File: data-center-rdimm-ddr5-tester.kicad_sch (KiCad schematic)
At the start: 2 parts

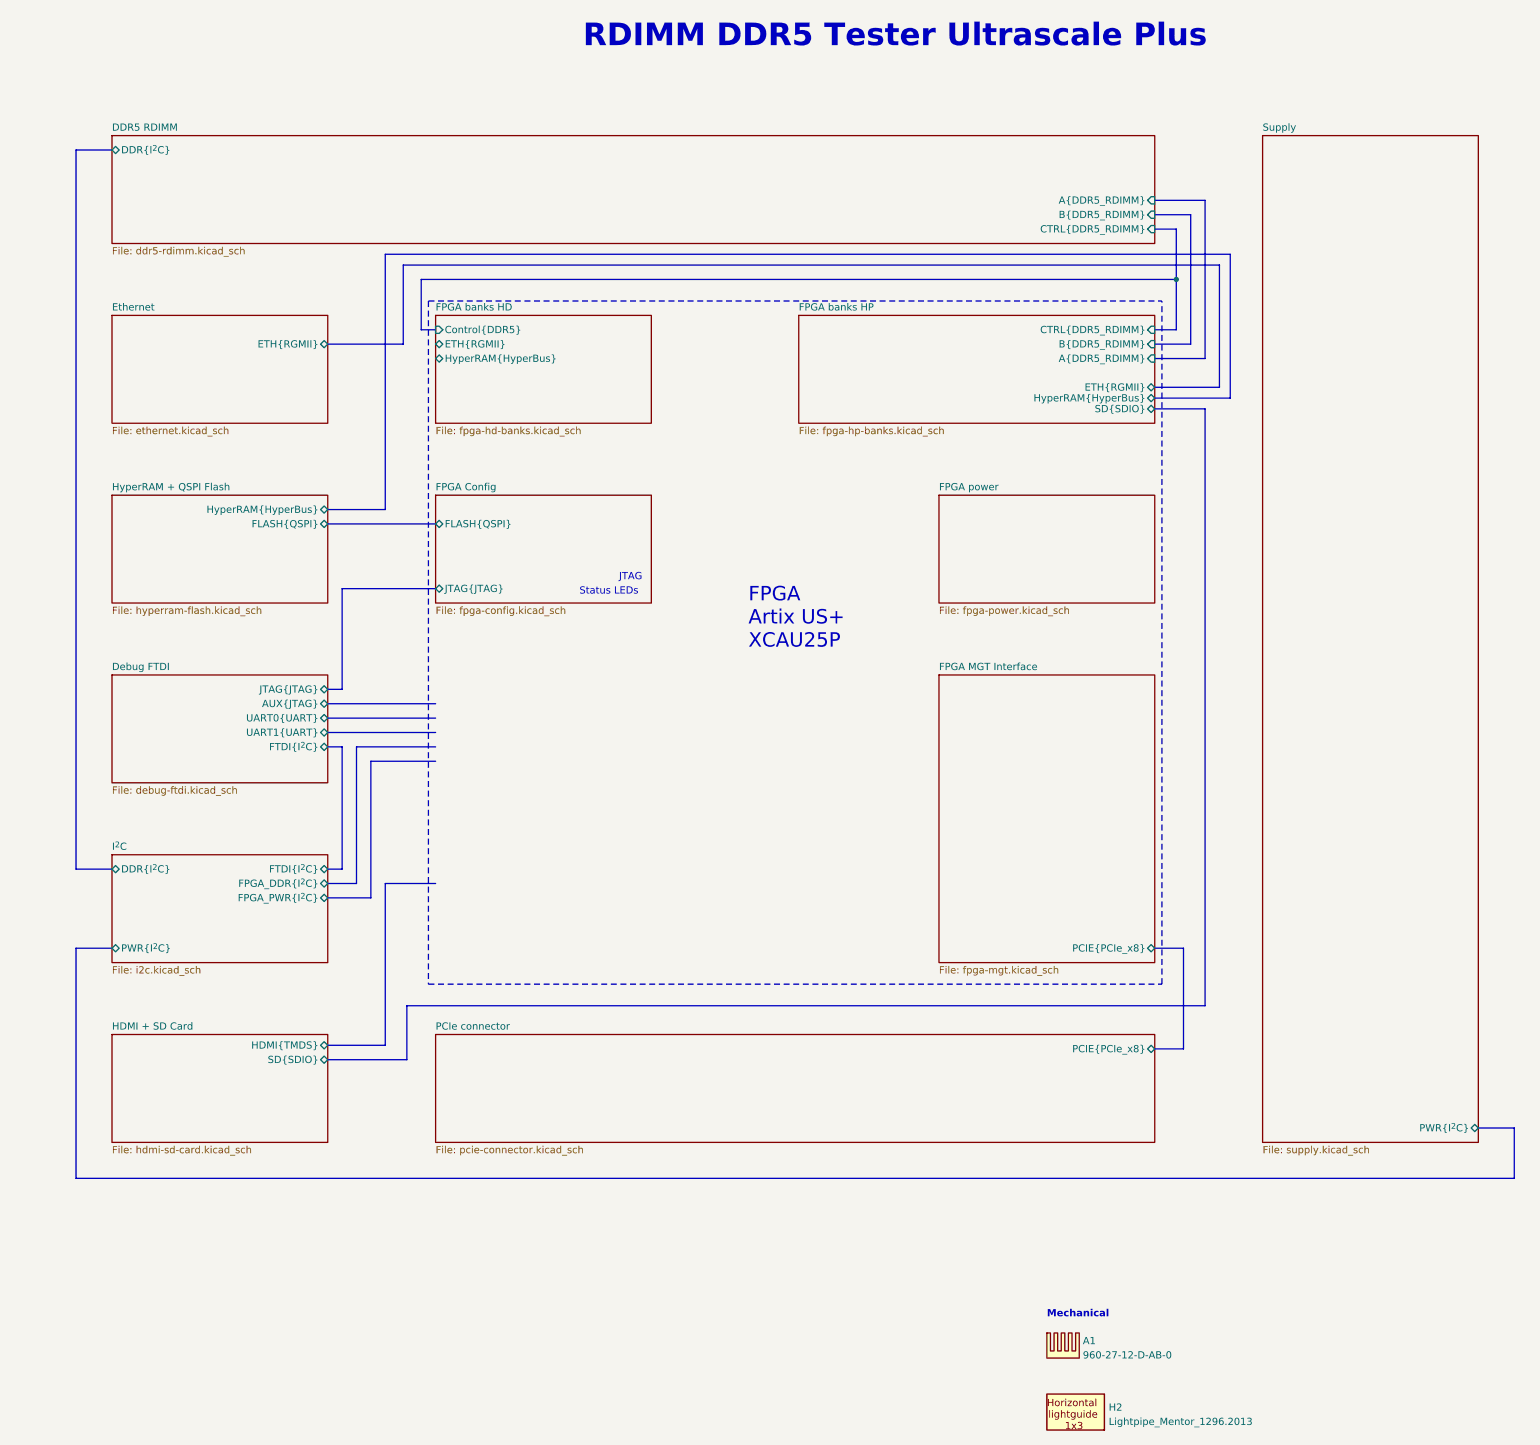
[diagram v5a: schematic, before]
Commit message: [#66312] Continued HDMI schematic connections
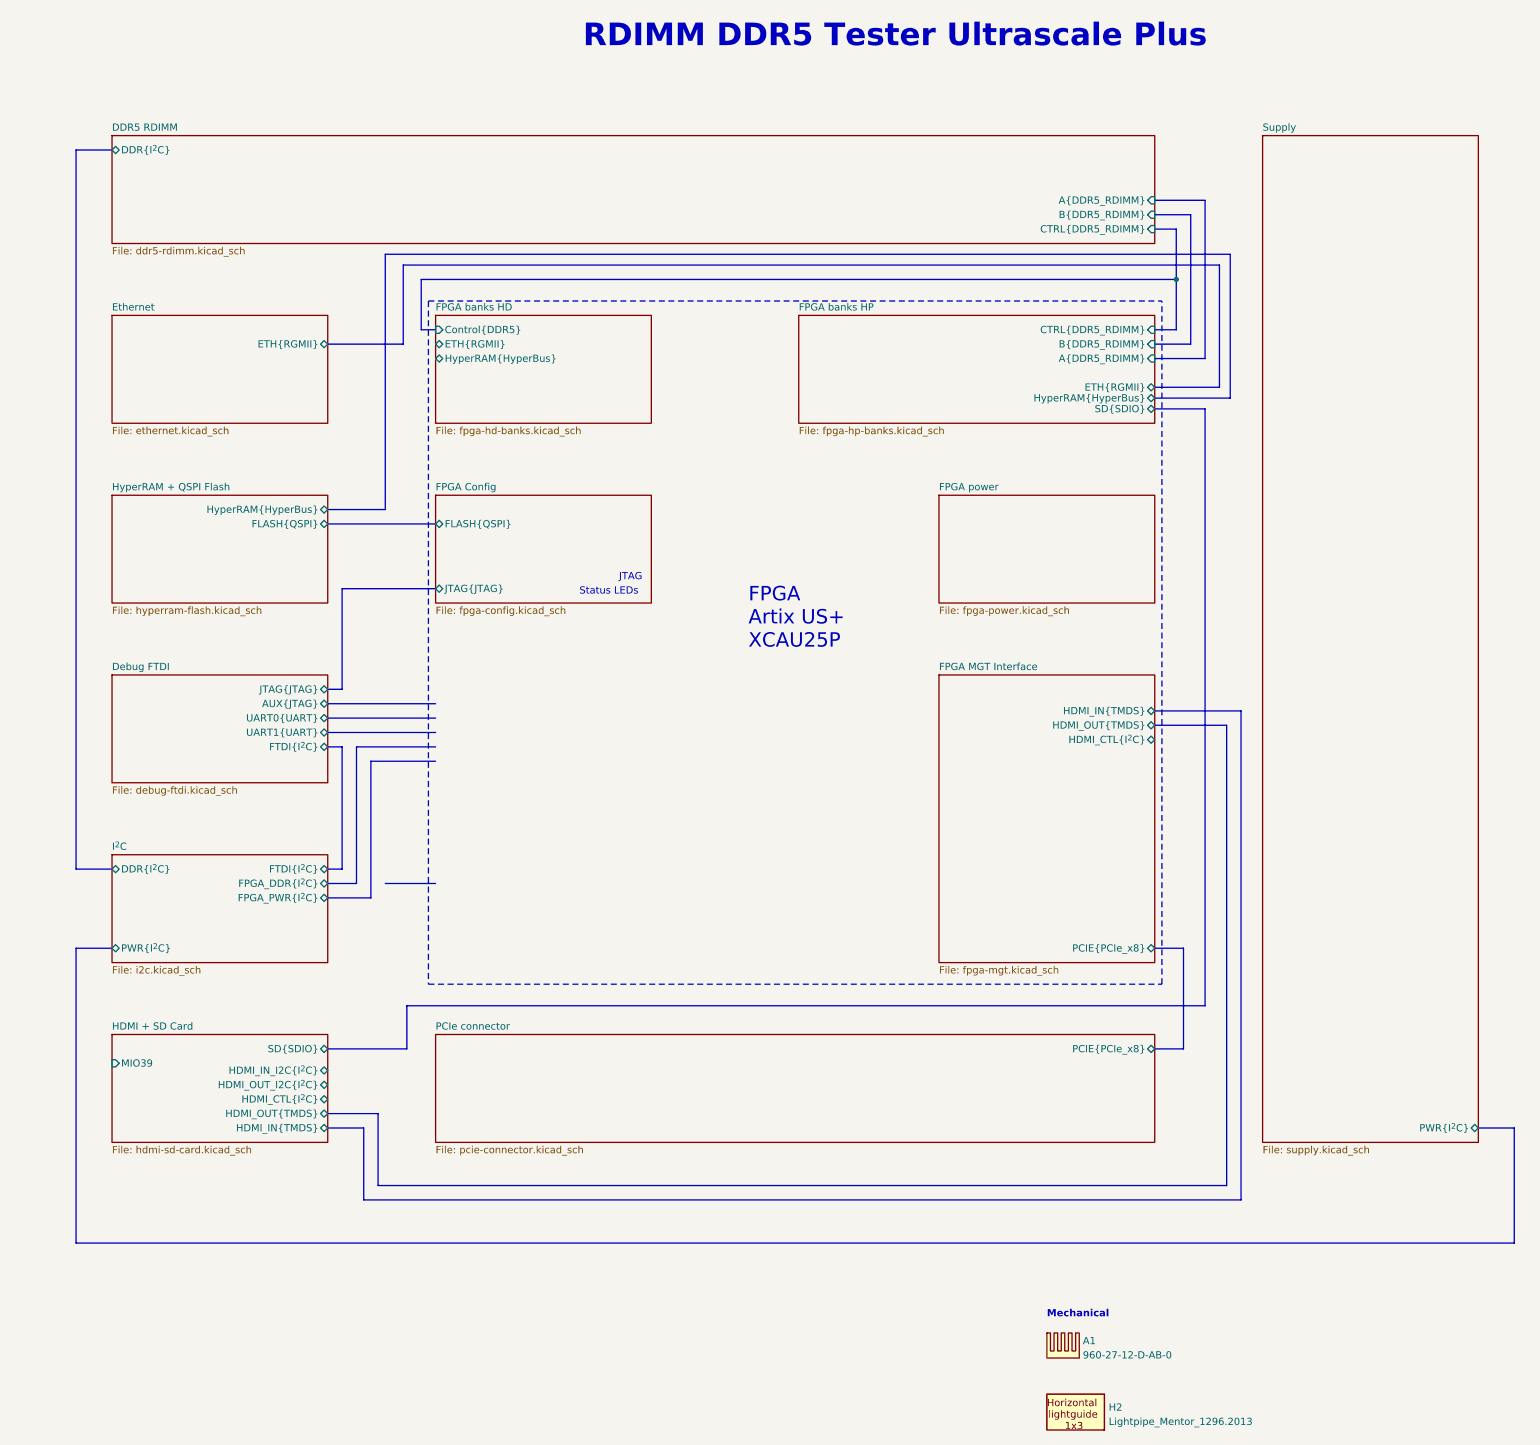
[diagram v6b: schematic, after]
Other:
- sheet FPGA MGT Interface ports: added HDMI_CTL{I^{2}C}, HDMI_IN{TMDS}, HDMI_OUT{TMDS}; removed none
- sheet HDMI + SD Card ports: added HDMI_CTL{I^{2}C}, HDMI_IN_I2C{I^{2}C}, HDMI_IN{TMDS}, HDMI_OUT_I2C{I^{2}C}, HDMI_OUT{TMDS}, MIO39; removed HDMI{TMDS}
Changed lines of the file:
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@@
     (stroke (width 0) (type default) (color 210 55 51 1))
   )
-  (bus (pts (xy 127 213.995) (xy 140.97 213.995))
+  (bus (pts (xy 135.89 223.52) (xy 135.89 236.22))
+    (stroke (width 0) (type default))
+  )
+  (bus (pts (xy 127 212.09) (xy 140.97 212.09))
     (stroke (width 0) (type default) (color 205 115 190 1))
-  )
-  (bus (pts (xy 137.16 182.88) (xy 137.16 211.455))
-    (stroke (width 0) (type default))
   )
   (bus (pts (xy 146.05 182.88) (xy 137.16 182.88))
@@
     (stroke (width 0) (type default) (color 210 55 51 1))
   )
+  (bus (pts (xy 273.05 152.4) (xy 288.29 152.4))
+    (stroke (width 0) (type default))
+  )
   (bus (pts (xy 140.335 73.66) (xy 284.48 73.66))
     (stroke (width 0) (type default) (color 210 55 51 1))
   )
-  (bus (pts (xy 82.55 234.95) (xy 336.55 234.95))
+  (bus (pts (xy 288.29 152.4) (xy 288.29 238.76))
+    (stroke (width 0) (type default))
+  )
+  (bus (pts (xy 82.55 246.38) (xy 336.55 246.38))
     (stroke (width 0) (type default))
   )
@@
     (stroke (width 0) (type default) (color 210 55 51 1))
   )
+  (bus (pts (xy 135.89 236.22) (xy 285.75 236.22))
+    (stroke (width 0) (type default))
+  )
   (bus (pts (xy 273.05 64.77) (xy 279.4 64.77))
     (stroke (width 0) (type default))
@@
     (stroke (width 0) (type default) (color 208 190 93 1))
   )
+  (bus (pts (xy 133.35 226.06) (xy 127 226.06))
+    (stroke (width 0) (type default))
+  )
   (bus (pts (xy 278.13 212.09) (xy 273.05 212.09))
     (stroke (width 0) (type default))
@@
     (stroke (width 0) (type default))
   )
+  (bus (pts (xy 285.75 154.94) (xy 273.05 154.94))
+    (stroke (width 0) (type default))
+  )
   (bus (pts (xy 129.54 130.81) (xy 129.54 148.59))
     (stroke (width 0) (type default))
@@
     (stroke (width 0) (type default))
   )
+  (bus (pts (xy 133.35 238.76) (xy 133.35 226.06))
+    (stroke (width 0) (type default))
+  )
   (bus (pts (xy 127 158.75) (xy 129.54 158.75))
     (stroke (width 0) (type default))
   )
   (bus (pts (xy 273.05 194.31) (xy 278.13 194.31))
-    (stroke (width 0) (type default))
-  )
-  (bus (pts (xy 137.16 211.455) (xy 127 211.455))
     (stroke (width 0) (type default))
   )
@@
     (stroke (width 0) (type default) (color 205 115 190 1))
   )
+  (bus (pts (xy 288.29 238.76) (xy 133.35 238.76))
+    (stroke (width 0) (type default))
+  )
   (bus (pts (xy 82.55 180.34) (xy 82.55 53.34))
     (stroke (width 0) (type default))
@@
     (stroke (width 0) (type default))
   )
-  (bus (pts (xy 336.55 226.06) (xy 336.55 234.95))
+  (bus (pts (xy 336.55 226.06) (xy 336.55 246.38))
     (stroke (width 0) (type default))
   )
@@
     (stroke (width 0) (type default) (color 210 55 51 1))
   )
-  (bus (pts (xy 140.97 204.47) (xy 140.97 213.995))
+  (bus (pts (xy 140.97 204.47) (xy 140.97 212.09))
     (stroke (width 0) (type default) (color 205 115 190 1))
   )
-  (bus (pts (xy 82.55 194.31) (xy 82.55 234.95))
+  (bus (pts (xy 285.75 236.22) (xy 285.75 154.94))
+    (stroke (width 0) (type default))
+  )
+  (bus (pts (xy 82.55 194.31) (xy 82.55 246.38))
     (stroke (width 0) (type default))
   )
@@
   )
   (bus (pts (xy 281.94 90.17) (xy 281.94 62.23))
+    (stroke (width 0) (type default))
+  )
+  (bus (pts (xy 127 223.52) (xy 135.89 223.52))
     (stroke (width 0) (type default))
   )
@@
       (effects (font (size 1.27 1.27)) (justify left top))
     )
-    (pin "HDMI{TMDS}" bidirectional (at 127 211.455 0)
-      (effects (font (size 1.27 1.27)) (justify right))
-    )
-    (pin "SD{SDIO}" bidirectional (at 127 213.995 0)
+    (pin "SD{SDIO}" bidirectional (at 127 212.09 0)
+      (effects (font (size 1.27 1.27)) (justify right))
+    )
+    (pin "HDMI_OUT{TMDS}" bidirectional (at 127 223.52 0)
+      (effects (font (size 1.27 1.27)) (justify right))
+    )
+    (pin "MIO39" input (at 88.9 214.63 180)
+      (effects (font (size 1.27 1.27)) (justify left))
+    )
+    (pin "HDMI_IN{TMDS}" bidirectional (at 127 226.06 0)
+      (effects (font (size 1.27 1.27)) (justify right))
+    )
+    (pin "HDMI_CTL{I^{2}C}" bidirectional (at 127 220.98 0)
+      (effects (font (size 1.27 1.27)) (justify right))
+    )
+    (pin "HDMI_OUT_I2C{I^{2}C}" bidirectional (at 127 218.44 0)
+      (effects (font (size 1.27 1.27)) (justify right))
+    )
+    (pin "HDMI_IN_I2C{I^{2}C}" bidirectional (at 127 215.9 0)
       (effects (font (size 1.27 1.27)) (justify right))
     )
     (instances
       (project "data-center-rdimm-ddr5-tester"
-        (path "/1faa6543-e26a-4449-8bac-ee14b9f19e5f" (page "17"))
+        (path "/1faa6543-e26a-4449-8bac-ee14b9f19e5f" (page "18"))
       )
     )
@@
       (effects (font (size 1.27 1.27)) (justify right))
     )
+    (pin "HDMI_OUT{TMDS}" bidirectional (at 273.05 154.94 0)
+      (effects (font (size 1.27 1.27)) (justify right))
+    )
+    (pin "HDMI_IN{TMDS}" bidirectional (at 273.05 152.4 0)
+      (effects (font (size 1.27 1.27)) (justify right))
+    )
+    (pin "HDMI_CTL{I^{2}C}" bidirectional (at 273.05 157.48 0)
+      (effects (font (size 1.27 1.27)) (justify right))
+    )
